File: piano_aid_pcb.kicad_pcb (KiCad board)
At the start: 2 copper layers, 44.5 x 61 mm, 37 parts, among them J1 PJ-082BH, J2 796644-3, J3 DIN-5_180degree, J4 Conn_01x06_Female, J5 Micro_SD_Card_Det, J6 Conn_01x07_Female, U1 317030213, U2 6N138, U3 74AHCT1G125W5-7, U4 AZ1117-3.3

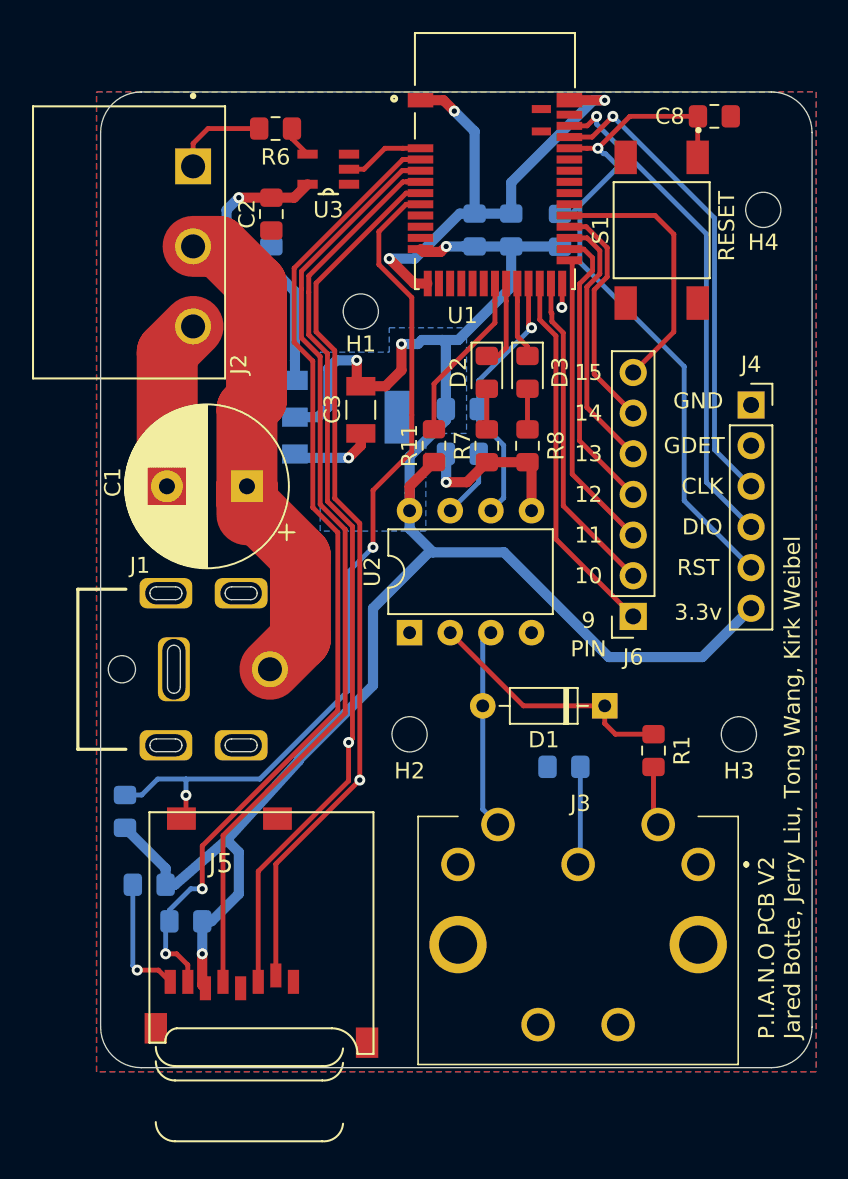
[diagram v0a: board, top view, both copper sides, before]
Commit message: Made final changes, added team/course number, fixed reset button pinout
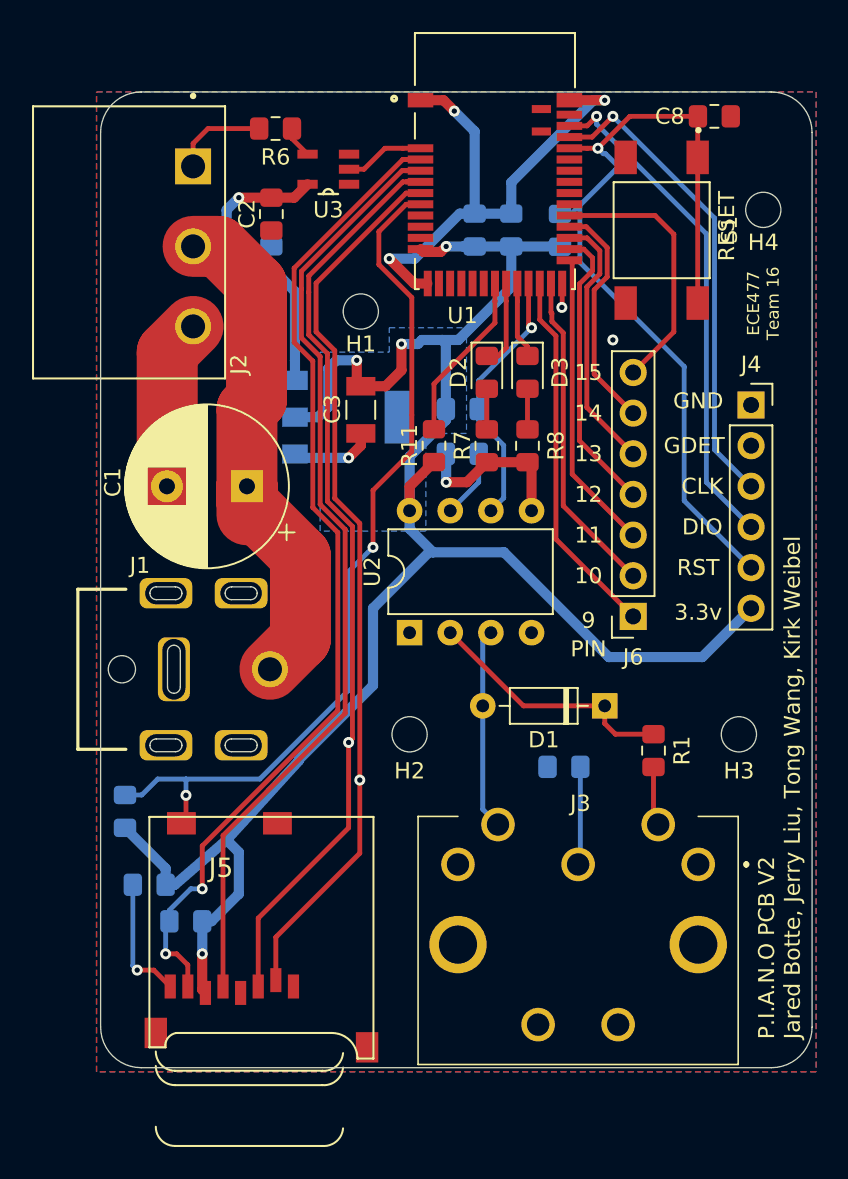
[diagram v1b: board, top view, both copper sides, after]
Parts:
- S1: value GPTS203211B -> 4-1437565-1
- moved J5 0.29 mm to (123.7, 118.9)
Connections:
- S1 pad 2: GND -> RESET
- S1 pad 3: (no net) -> GND
- S1 pad 4: (no net) -> GND
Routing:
- net RESET: track 45.4 -> 54.5 mm
- net GND: vias 6 -> 7
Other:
- board text added: "ECE477 Team 16"
- board text added: "ECE477 Team 16 P.I.A.N.O PCB V2 Jared Botte Jerry Liu Tong Wang Kirk Weibel"
- board text removed: "P.I.A.N.O PCB V2 Jared Botte Jerry Liu Tong Wang Kirk Weibel"

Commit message: Added via for button second ground
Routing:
- net GND: vias 7 -> 8

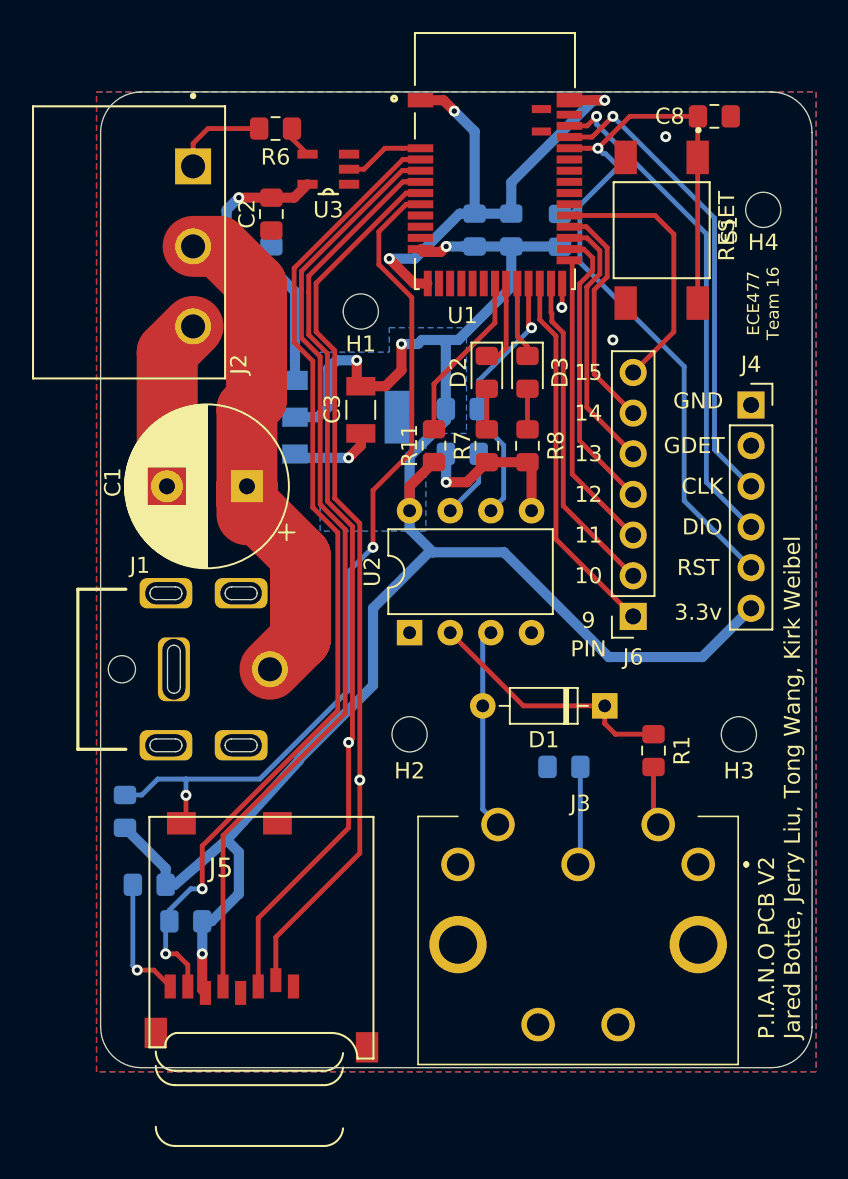
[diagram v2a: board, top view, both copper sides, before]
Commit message: Removed unused libraries to reduce project size
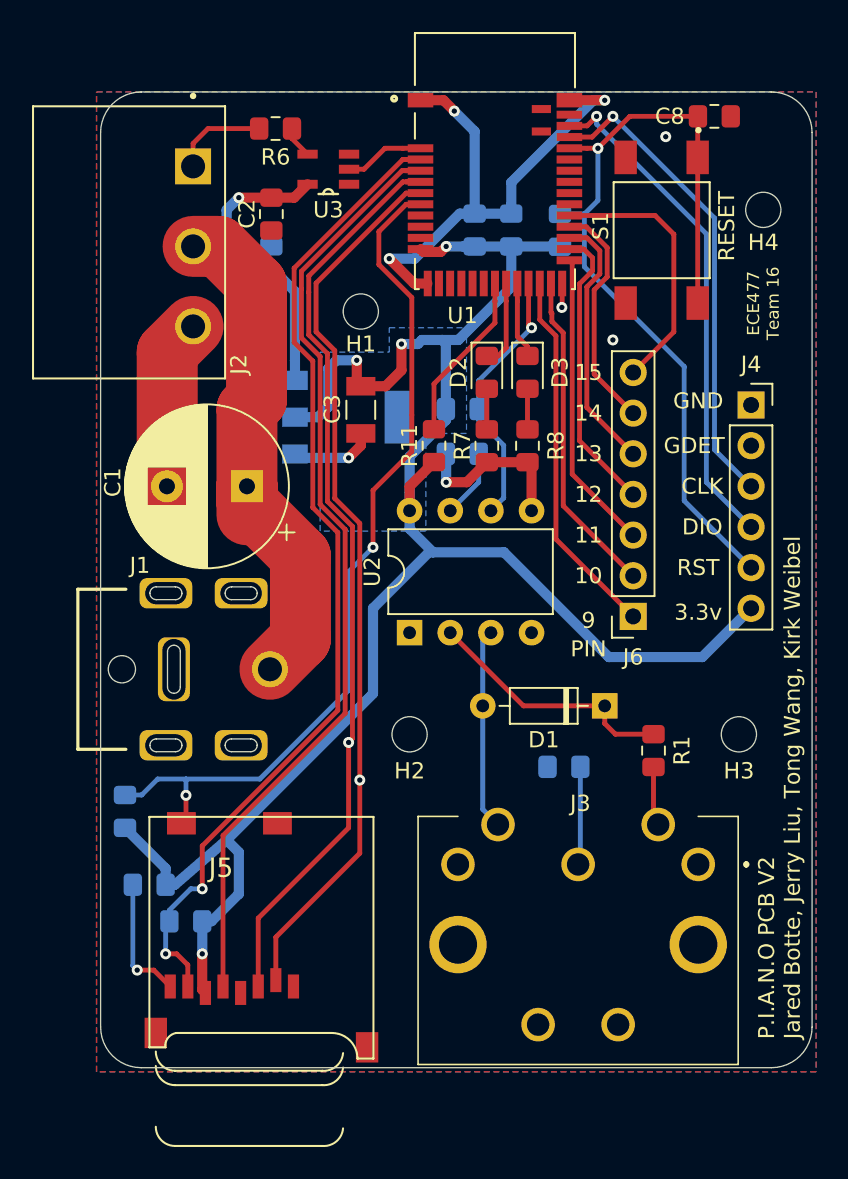
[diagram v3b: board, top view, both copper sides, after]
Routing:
- net RESET: track 54.5 -> 52.9 mm
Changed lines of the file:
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@@
     (thickness 1.6)
     (drawings 29)
-    (tracks 325)
+    (tracks 319)
     (zones 0)
     (modules 37)
@@
   )
   (setup
-    (last_trace_width 0.1524)
+    (last_trace_width 0.635)
     (user_trace_width 0.3048)
     (user_trace_width 0.635)
@@
   (module 4-1437565-1:SW_4-1437565-1 (layer F.Cu)
     (at 155.702 82.296 270)
-    (fp_text reference S1 (at -0.025 -4.235 90) (layer F.SilkS)
+    (fp_text reference S1 (at -0.254 3.81 90) (layer F.SilkS)
       (effects (font (size 1 1) (thickness 0.15)))
     )
@@
   (via (at 127 127.508) (size 0.6858) (drill 0.3302) (layers F.Cu B.Cu) (net 3))
   (segment (start 139.954 99.822) (end 139.954 100.95337) (width 0.635) (layer B.Cu) (net 3))
-  (segment (start 141.420315 102.419685) (end 141.166315 102.419685) (width 0.635) (layer B.Cu) (net 3))
   (segment (start 139.954 100.95337) (end 141.420315 102.419685) (width 0.635) (layer B.Cu) (net 3))
   (segment (start 125.289 123.19) (end 124.714 123.19) (width 0.635) (layer B.Cu) (net 3))
@@
   (segment (start 129.286 123.765) (end 129.286 121.158) (width 0.635) (layer B.Cu) (net 3))
   (segment (start 128.524 120.396) (end 125.289 123.19) (width 0.635) (layer B.Cu) (net 3))
-  (segment (start 133.029901 115.449099) (end 128.524 120.396) (width 0.635) (layer B.Cu) (net 3))
   (segment (start 127 125.476) (end 127 127.508) (width 0.635) (layer B.Cu) (net 3))
-  (segment (start 133.029901 115.382099) (end 137.668 110.744) (width 0.635) (layer B.Cu) (net 3))
-  (segment (start 137.668 105.918) (end 141.166315 102.419685) (width 0.635) (layer B.Cu) (net 3))
-  (segment (start 137.668 110.744) (end 137.668 105.918) (width 0.635) (layer B.Cu) (net 3))
   (segment (start 138.451 92.046) (end 139.446 91.051) (width 0.635) (layer F.Cu) (net 3))
   (segment (start 136.906 92.046) (end 138.451 92.046) (width 0.635) (layer F.Cu) (net 3))
@@
   (segment (start 139.954 98.307) (end 139.954 99.822) (width 0.635) (layer F.Cu) (net 3))
   (segment (start 141.478 96.783) (end 139.954 98.307) (width 0.635) (layer F.Cu) (net 3))
-  (segment (start 133.029901 115.449099) (end 133.029901 115.382099) (width 0.635) (layer B.Cu) (net 3))
   (segment (start 127 129.752) (end 127.198 129.95) (width 0.635) (layer F.Cu) (net 3))
   (segment (start 127 127.508) (end 127 129.752) (width 0.635) (layer F.Cu) (net 3))
+  (segment (start 141.166315 102.419685) (end 141.420315 102.419685) (width 0.635) (layer B.Cu) (net 3))
+  (segment (start 137.668 105.918) (end 141.166315 102.419685) (width 0.635) (layer B.Cu) (net 3))
+  (segment (start 128.524 120.396) (end 137.668 111.252) (width 0.635) (layer B.Cu) (net 3))
+  (segment (start 137.668 111.252) (end 137.668 105.918) (width 0.635) (layer B.Cu) (net 3))
   (segment (start 150.622 121.781) (end 150.483 121.92) (width 0.3048) (layer B.Cu) (net 4))
   (segment (start 150.622 115.824) (end 150.622 121.781) (width 0.3048) (layer B.Cu) (net 4))
@@
   (segment (start 157.97 75.184) (end 153.715358 75.184) (width 0.3048) (layer F.Cu) (net 13))
   (via (at 151.721358 77.178) (size 0.6858) (drill 0.3302) (layers F.Cu B.Cu) (net 13))
-  (segment (start 149.352 81.28) (end 150.052 81.28) (width 0.3048) (layer B.Cu) (net 13))
-  (segment (start 152.846 78.486) (end 153.162 78.486) (width 0.3048) (layer B.Cu) (net 13))
-  (segment (start 152.196899 77.520899) (end 153.162 78.486) (width 0.3048) (layer B.Cu) (net 13))
-  (segment (start 152.064257 77.520899) (end 152.196899 77.520899) (width 0.3048) (layer B.Cu) (net 13))
-  (segment (start 151.721358 77.178) (end 152.064257 77.520899) (width 0.3048) (layer B.Cu) (net 13))
-  (segment (start 150.591 80.741) (end 150.591 84.297) (width 0.3048) (layer B.Cu) (net 13))
-  (segment (start 150.591 80.741) (end 152.846 78.486) (width 0.3048) (layer B.Cu) (net 13))
-  (segment (start 150.052 81.28) (end 150.591 80.741) (width 0.3048) (layer B.Cu) (net 13))
   (segment (start 157.110801 99.198801) (end 161.29 103.378) (width 0.3048) (layer B.Cu) (net 13))
   (segment (start 157.110801 90.816801) (end 157.110801 99.198801) (width 0.3048) (layer B.Cu) (net 13))
-  (segment (start 150.591 84.297) (end 157.110801 90.816801) (width 0.3048) (layer B.Cu) (net 13))
   (segment (start 157.952 77.746) (end 157.952 86.846) (width 0.3048) (layer F.Cu) (net 13))
+  (segment (start 150.876 81.28) (end 150.876 84.582) (width 0.3048) (layer B.Cu) (net 13))
+  (segment (start 150.876 81.28) (end 149.352 81.28) (width 0.3048) (layer B.Cu) (net 13))
+  (segment (start 150.876 84.582) (end 157.110801 90.816801) (width 0.3048) (layer B.Cu) (net 13))
+  (segment (start 151.721358 80.434642) (end 150.876 81.28) (width 0.3048) (layer B.Cu) (net 13))
+  (segment (start 151.721358 77.178) (end 151.721358 80.434642) (width 0.3048) (layer B.Cu) (net 13))
   (segment (start 122.664 123.19) (end 122.664 128.252) (width 0.3048) (layer B.Cu) (net 14))
   (via (at 122.936 128.524) (size 0.6858) (drill 0.3302) (layers F.Cu B.Cu) (net 14))

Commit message: Added 1206 fuse
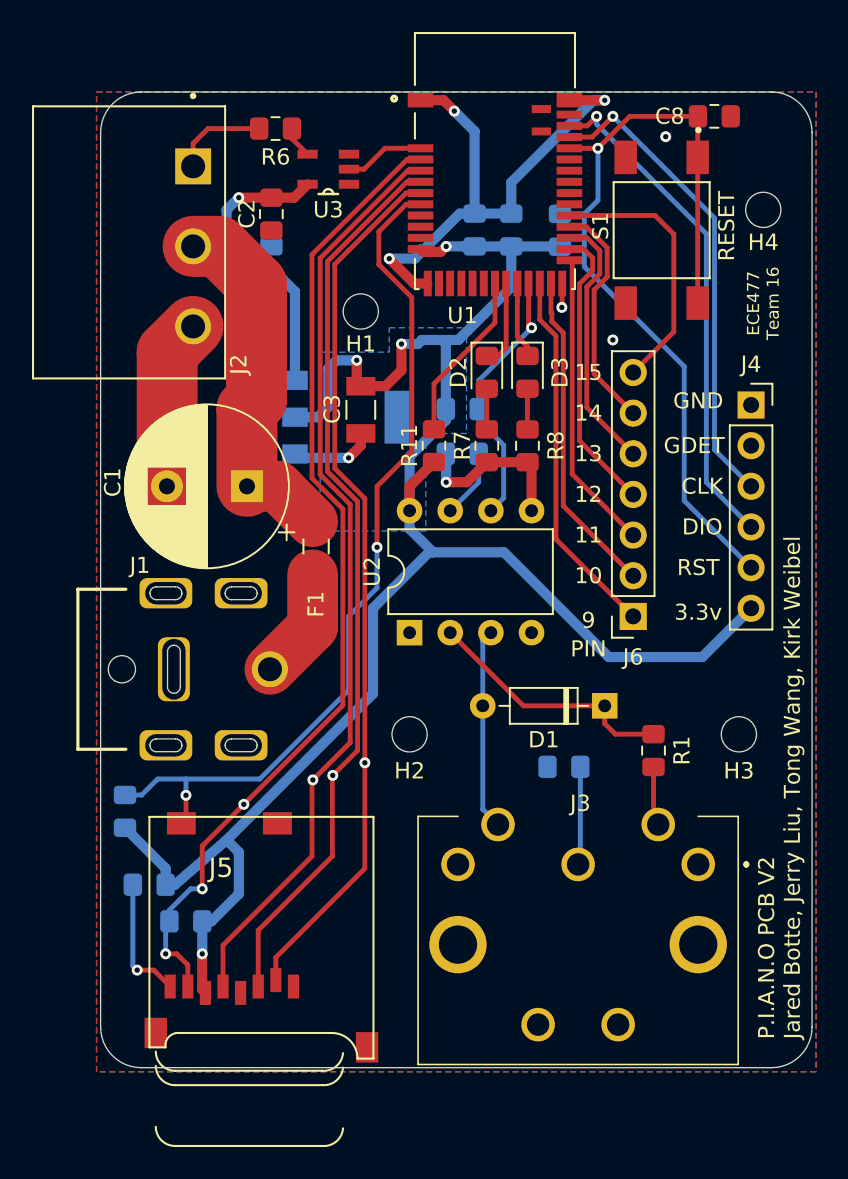
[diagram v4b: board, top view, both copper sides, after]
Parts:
- added F1: 0685P8000-01, 0685P8000-01:FUSC3215X83N, F.Cu at (134.1, 102.1)
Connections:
- J1 pad 1: 5V -> Net-(F1-Pad1)
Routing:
- net 5V: track 55.1 -> 44.0 mm
- net Net-(F1-Pad1): track 0.00 -> 7.00 mm
- net CLK: track 60.0 -> 58.1 mm, vias 0 -> 1
- net CMD: track 58.3 -> 56.5 mm
- net DAT0: track 63.5 -> 61.8 mm, vias 2 -> 3
- net CD: track 55.7 -> 55.0 mm

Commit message: Added reccomended vias
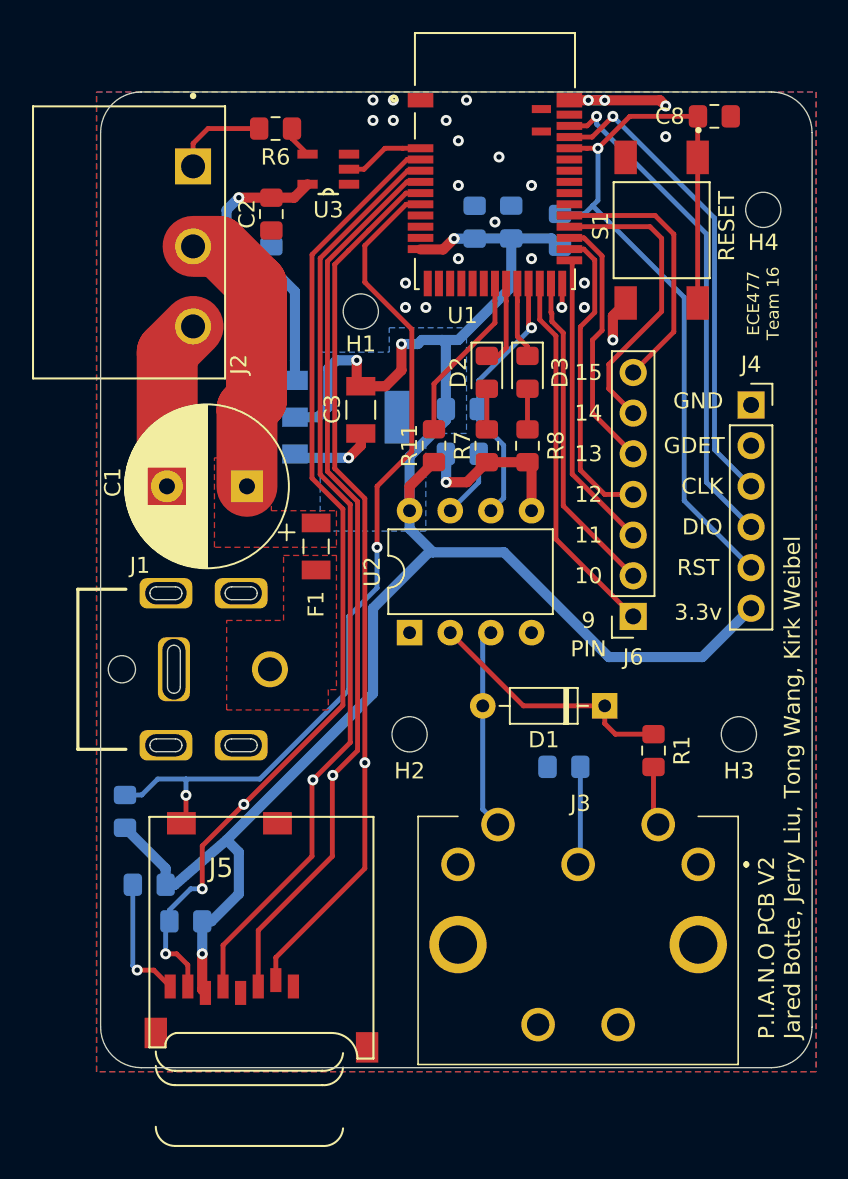
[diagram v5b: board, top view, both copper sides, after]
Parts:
- moved C6 0.50 mm to (146.3, 81.8)
- moved C7 0.49 mm to (144.0, 81.8)
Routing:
- net GND: track 61.3 -> 37.5 mm, vias 8 -> 26
- net Net-(F1-Pad1): track 7.00 -> 0.00 mm
- net 5V: track 44.0 -> 39.0 mm
- net P14: track 14.6 -> 19.0 mm
- net P12: track 18.2 -> 19.3 mm
- net 3.3V: track 119.4 -> 120.3 mm
- net DET: track 53.7 -> 54.4 mm
- added copper zone on F.Cu, net 5V
- added copper zone on F.Cu, net Net-(F1-Pad1)
